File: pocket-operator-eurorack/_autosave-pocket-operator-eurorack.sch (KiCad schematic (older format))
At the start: 28 parts, among them J1 Conn_02x05_Odd_Even, J10 Conn_01x01, J11 Conn_01x01, J12 Conn_01x01, J13 Conn_01x01, J6 Conn_01x01, J7 Conn_01x01, J8 Conn_01x01, J9 Conn_01x01, U1 NCP1117-3.3_SOT223

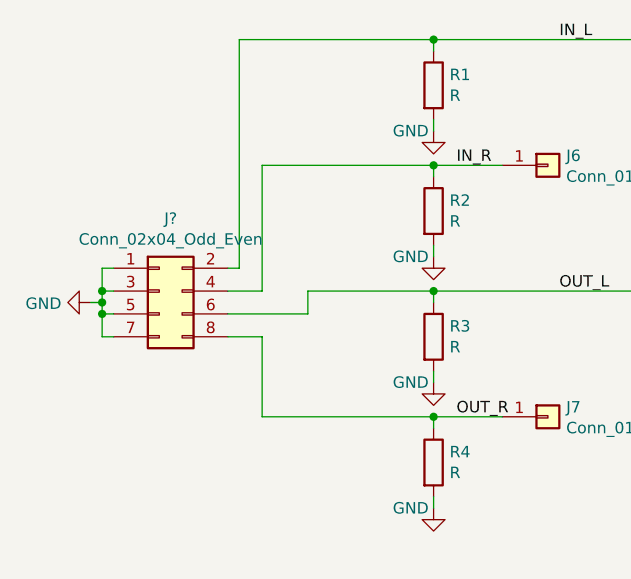
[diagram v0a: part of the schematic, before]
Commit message: components selected and placed on board, need to confirm that gnds are connector to each other and that in/out pads are placed correctly
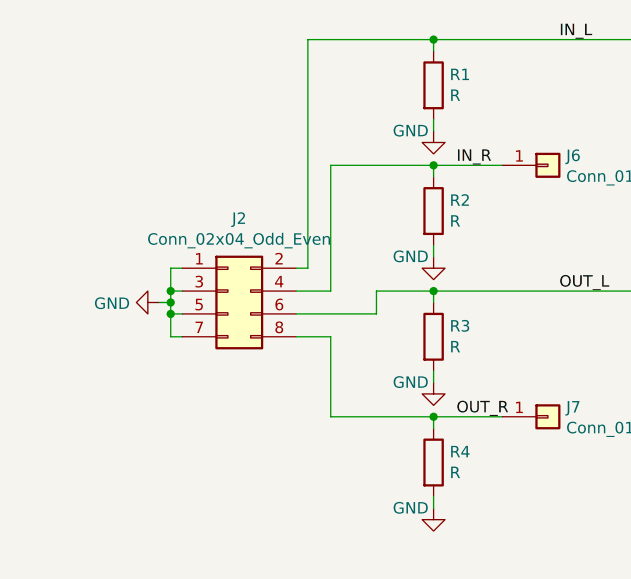
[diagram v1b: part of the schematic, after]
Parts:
- gave numbers to parts that had none: 1
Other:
- moved on the sheet: J2
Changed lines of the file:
@@
 	2400 2950 2400 2900
 Wire Wire Line
-	1850 2350 2400 2350
+	2150 2350 2400 2350
 Connection ~ 2400 2350
 Wire Wire Line
@@
 OUT_R
 $Comp
-L Connector_Generic:Conn_02x04_Odd_Even J?
+L Connector_Generic:Conn_02x04_Odd_Even J2
 U 1 1 61CBB0A8
-P 1200 2350
-F 0 "J?" H 1250 2667 50  0000 C CNN
-F 1 "Conn_02x04_Odd_Even" H 1250 2576 50  0000 C CNN
-F 2 "Connector_PinSocket_2.54mm:PinSocket_2x04_P2.54mm_Vertical" H 1200 2350 50  0001 C CNN
-F 3 "~" H 1200 2350 50  0001 C CNN
-	1    1200 2350
+P 1500 2350
+F 0 "J2" H 1550 2667 50  0000 C CNN
+F 1 "Conn_02x04_Odd_Even" H 1550 2576 50  0000 C CNN
+F 2 "Connector_PinSocket_2.54mm:PinSocket_2x04_P2.54mm_Vertical" H 1500 2350 50  0001 C CNN
+F 3 "~" H 1500 2350 50  0001 C CNN
+	1    1500 2350
 	1    0    0    -1
 $EndComp
 Wire Wire Line
-	1000 2250 950  2250
+	1300 2250 1250 2250
 Wire Wire Line
-	950  2250 950  2350
+	1250 2250 1250 2350
 Wire Wire Line
-	950  2550 1000 2550
+	1250 2550 1300 2550
 Wire Wire Line
-	1000 2450 950  2450
-Connection ~ 950  2450
+	1300 2450 1250 2450
+Connection ~ 1250 2450
 Wire Wire Line
-	950  2450 950  2550
+	1250 2450 1250 2550
 Wire Wire Line
-	950  2350 1000 2350
-Connection ~ 950  2350
+	1250 2350 1300 2350
+Connection ~ 1250 2350
 Wire Wire Line
-	950  2350 950  2400
+	1250 2350 1250 2400
 $Comp
-L power:GND #PWR?
+L power:GND #PWR0101
 U 1 1 61CCE36B
-P 900 2400
-F 0 "#PWR?" H 900 2150 50  0001 C CNN
-F 1 "GND" V 905 2272 50  0000 R CNN
-F 2 "" H 900 2400 50  0001 C CNN
-F 3 "" H 900 2400 50  0001 C CNN
-	1    900  2400
+P 1200 2400
+F 0 "#PWR0101" H 1200 2150 50  0001 C CNN
+F 1 "GND" V 1205 2272 50  0000 R CNN
+F 2 "" H 1200 2400 50  0001 C CNN
+F 3 "" H 1200 2400 50  0001 C CNN
+	1    1200 2400
 	0    1    1    0
 $EndComp
 Wire Wire Line
-	900  2400 950  2400
-Connection ~ 950  2400
+	1200 2400 1250 2400
+Connection ~ 1250 2400
 Wire Wire Line
-	950  2400 950  2450
+	1250 2400 1250 2450
 Wire Wire Line
-	1500 2250 1550 2250
+	1800 2250 1850 2250
 Wire Wire Line
-	1550 2250 1550 1250
+	1850 2250 1850 1250
 Wire Wire Line
-	1550 1250 2400 1250
+	1850 1250 2400 1250
 Wire Wire Line
-	1650 1800 1650 2350
+	1950 1800 1950 2350
 Wire Wire Line
-	1650 2350 1500 2350
+	1950 2350 1800 2350
 Wire Wire Line
-	1650 1800 2400 1800
+	1950 1800 2400 1800
 Wire Wire Line
-	1850 2350 1850 2450
+	2150 2350 2150 2450
 Wire Wire Line
-	1850 2450 1500 2450
+	2150 2450 1800 2450
 Wire Wire Line
-	1500 2550 1650 2550
+	1800 2550 1950 2550
 Wire Wire Line
-	1650 2550 1650 2900
+	1950 2550 1950 2900
 Wire Wire Line
-	1650 2900 2400 2900
+	1950 2900 2400 2900
 $EndSCHEMATC
